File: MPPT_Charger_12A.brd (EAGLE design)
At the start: 100 x 80 mm, 113 parts, among them IC1 LM358D, Q1 IRFR3607, Q2 IRFR3607, Q3 IRFR3607, Q5 IRFR3607, Q7 ZXMP10A13FTA, T1 MMBT3904, U1 SN65HVD230, U2 INA199A1DCKR, U3 LM5101A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

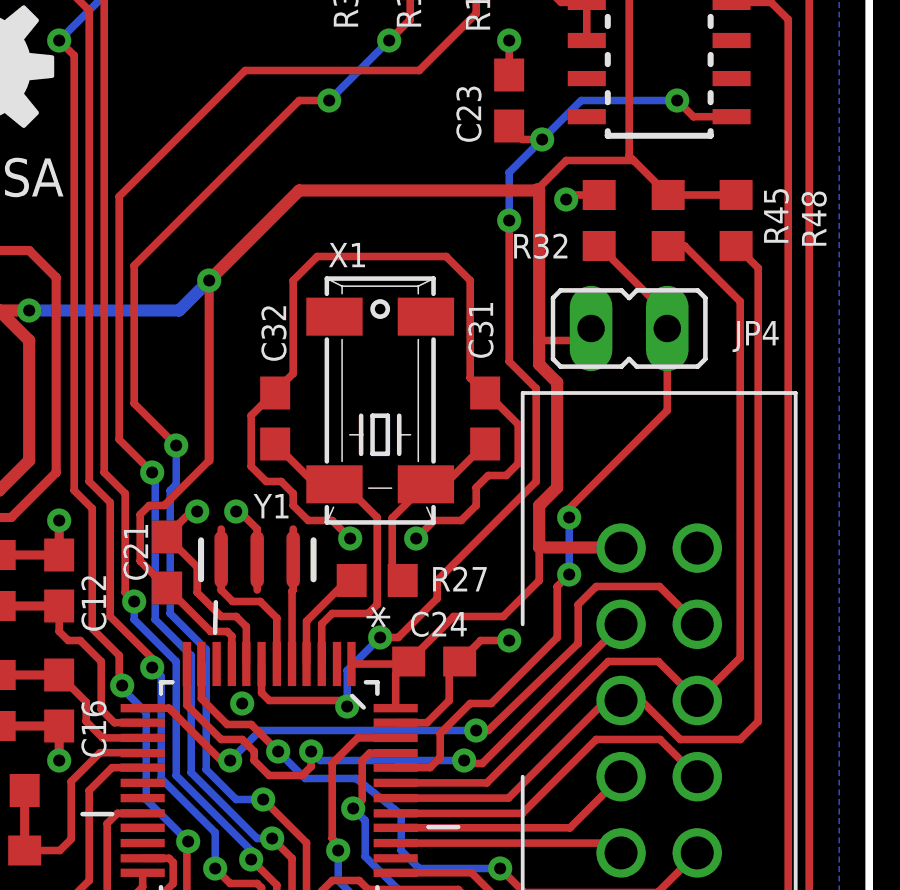
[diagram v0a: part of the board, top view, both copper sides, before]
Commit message: Fixed clearance at some vias (DRC error)
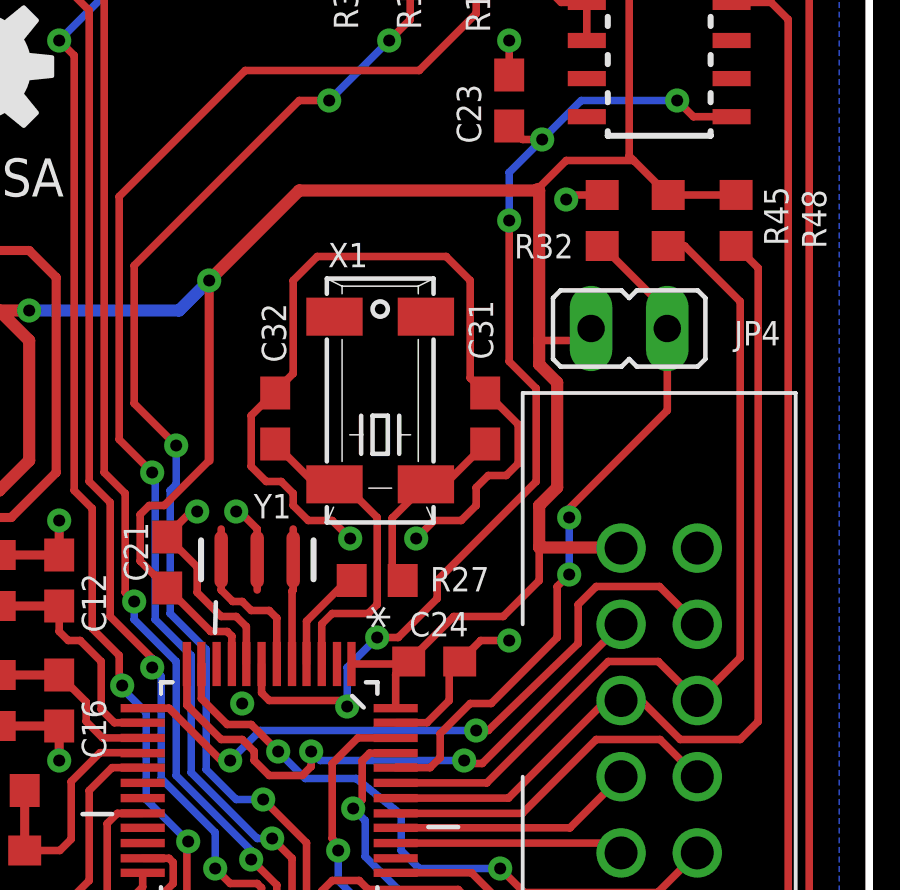
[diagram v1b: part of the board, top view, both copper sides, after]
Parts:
- moved R32 0.10 mm to (91.1, 59.0)
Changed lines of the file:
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@@
 <layer number="49" name="Reference" color="13" fill="1" visible="no" active="yes"/>
 <layer number="50" name="dxf" color="12" fill="1" visible="no" active="yes"/>
-<layer number="51" name="tDocu" color="7" fill="1" visible="no" active="yes"/>
+<layer number="51" name="tDocu" color="7" fill="1" visible="yes" active="yes"/>
 <layer number="52" name="bDocu" color="7" fill="1" visible="no" active="yes"/>
 <layer number="57" name="tCAD" color="7" fill="1" visible="no" active="no"/>
@@
 <attribute name="VALUE" x="94.54" y="58.321" size="1.27" layer="27" ratio="10" rot="R180"/>
 </element>
-<element name="R32" library="rcl" package="R0603" value="10k" x="91" y="59" smashed="yes" rot="R270">
-<attribute name="MPN" value="RC0603FR-0710KL" x="91" y="59" size="1.778" layer="27" rot="R270" display="off"/>
-<attribute name="MF" value="YAGEO (PHYCOMP)" x="91" y="59" size="1.778" layer="27" rot="R270" display="off"/>
-<attribute name="OC_FARNELL" value="9238603" x="91" y="59" size="1.778" layer="27" rot="R270" display="off"/>
-<attribute name="NAME" x="88.065" y="57.735" size="0.8128" layer="25"/>
-<attribute name="VALUE" x="89.095" y="59.635" size="1.27" layer="27" rot="R270"/>
+<element name="R32" library="rcl" package="R0603" value="10k" x="91.1" y="59" smashed="yes" rot="R270">
+<attribute name="MPN" value="RC0603FR-0710KL" x="91.1" y="59" size="1.778" layer="27" rot="R270" display="off"/>
+<attribute name="MF" value="YAGEO (PHYCOMP)" x="91.1" y="59" size="1.778" layer="27" rot="R270" display="off"/>
+<attribute name="OC_FARNELL" value="9238603" x="91.1" y="59" size="1.778" layer="27" rot="R270" display="off"/>
+<attribute name="NAME" x="88.165" y="57.735" size="0.8128" layer="25"/>
+<attribute name="VALUE" x="89.195" y="59.635" size="1.27" layer="27" rot="R270"/>
 </element>
 <element name="LED3" library="SparkFun-LED" package="LED3MM" value="" x="76" y="75" smashed="yes">
@@
 <wire x1="87.05" y1="45" x2="88" y2="45" width="0.254" layer="1"/>
 <via x="89.9" y="59.7" extent="1-16" drill="0.4"/>
-<wire x1="91" y1="59.85" x2="90.05" y2="59.85" width="0.254" layer="1"/>
+<wire x1="91.1" y1="59.85" x2="90.05" y2="59.85" width="0.254" layer="1"/>
 <wire x1="90.05" y1="59.85" x2="89.9" y2="59.7" width="0.254" layer="1"/>
 <via x="89" y="67" extent="1-16" drill="0.4"/>
@@
 <wire x1="85.6" y1="47" x2="85.6" y2="46.4" width="0.254" layer="1"/>
 <wire x1="85.6" y1="46.4" x2="84.3" y2="45.1" width="0.254" layer="1"/>
-<wire x1="84.3" y1="45.1" x2="83.7" y2="45.1" width="0.254" layer="1"/>
-<via x="83.7" y="45.1" extent="1-16" drill="0.4"/>
-<wire x1="83.7" y1="45.1" x2="82.6" y2="44" width="0.254" layer="16"/>
-<wire x1="82.6" y1="44" x2="82.6" y2="42.8" width="0.254" layer="16"/>
+<wire x1="84.3" y1="45.1" x2="83.6" y2="45.1" width="0.254" layer="1"/>
+<via x="83.6" y="45.1" extent="1-16" drill="0.4"/>
+<wire x1="83.6" y1="45.1" x2="82.6" y2="44.1" width="0.254" layer="16"/>
+<wire x1="82.6" y1="44.1" x2="82.6" y2="42.8" width="0.254" layer="16"/>
 <via x="82.6" y="42.8" extent="1-16" drill="0.4"/>
 <wire x1="82.6" y1="42.8" x2="82.4" y2="43" width="0.254" layer="1"/>
@@
 <via x="90" y="49.1" extent="1-16" drill="0.4"/>
 <wire x1="90" y1="49.1" x2="90" y2="49.4" width="0.254" layer="1"/>
-<wire x1="91" y1="58.15" x2="93.27" y2="55.88" width="0.254" layer="1"/>
-<wire x1="93.27" y1="55.88" x2="93.27" y2="55.4" width="0.254" layer="1"/>
+<wire x1="91.1" y1="58.15" x2="93.27" y2="55.98" width="0.254" layer="1"/>
+<wire x1="93.27" y1="55.98" x2="93.27" y2="55.4" width="0.254" layer="1"/>
 <wire x1="90" y1="49.4" x2="93.27" y2="52.67" width="0.254" layer="1"/>
 <wire x1="93.27" y1="52.67" x2="93.27" y2="55.4" width="0.254" layer="1"/>
@@
 <contactref element="Y1" pad="3"/>
 <wire x1="80.254" y1="44.2164" x2="80.254" y2="45.746" width="0.254" layer="1"/>
-<wire x1="80.254" y1="45.746" x2="79.7" y2="46.3" width="0.254" layer="1"/>
-<wire x1="79.7" y1="46.3" x2="78.784" y2="46.3" width="0.254" layer="1"/>
 <wire x1="78.784" y1="46.3" x2="78.4" y2="46.684" width="0.254" layer="1"/>
+<wire x1="78.784" y1="46.3" x2="79.1" y2="46.3" width="0.254" layer="1"/>
+<wire x1="79.1" y1="46.3" x2="79.4" y2="46" width="0.254" layer="1"/>
+<wire x1="79.4" y1="46" x2="80" y2="46" width="0.254" layer="1"/>
+<wire x1="80" y1="46" x2="80.254" y2="45.746" width="0.254" layer="1"/>
 </signal>
 </signals>
